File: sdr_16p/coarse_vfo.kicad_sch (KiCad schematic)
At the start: 1 part, among them U8 ADF4351

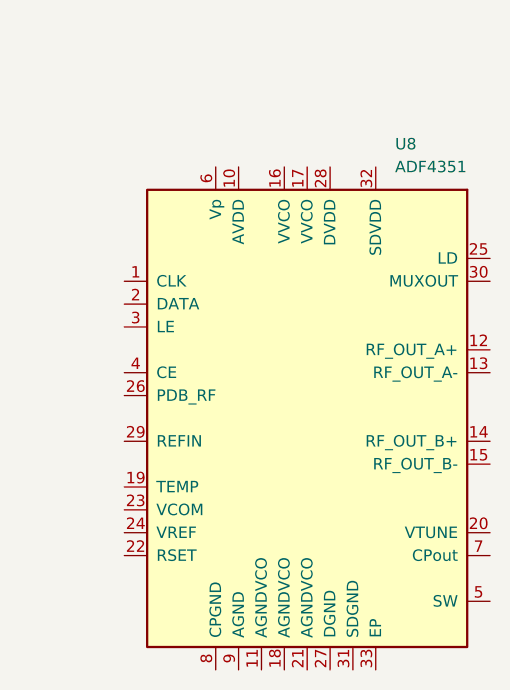
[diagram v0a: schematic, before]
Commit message: back to 16 phases
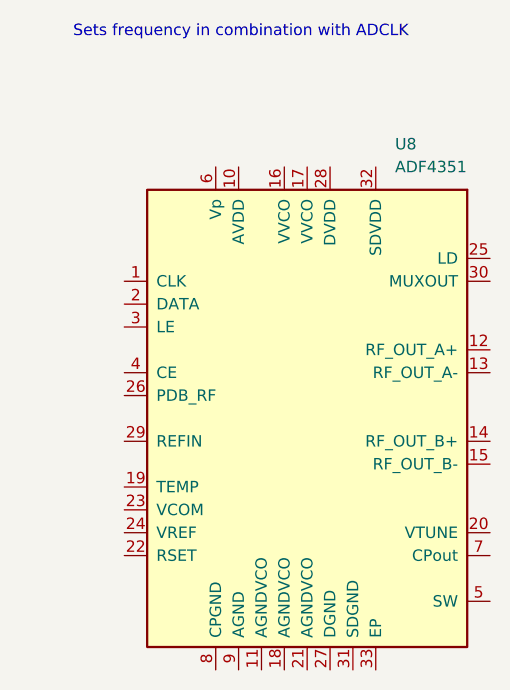
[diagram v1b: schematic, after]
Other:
- note added: "Sets frequency in combination with ADCLK"
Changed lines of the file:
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@@
 		(company "Andy McCann KA3KAF and Doug McCann KA3KAG")
+	)
+	(text "Sets frequency in combination with ADCLK"
+		(exclude_from_sim no)
+		(at 221.234 80.264 0)
+		(effects
+			(font
+				(size 1.27 1.27)
+			)
+		)
 	)
 	(symbol
